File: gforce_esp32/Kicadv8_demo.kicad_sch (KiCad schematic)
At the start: 26 parts, among them J1 USB_C_Receptacle, SW1 TL3215AF160BQ, SW2 TL3215AF160RQ, U1 ESP32-S3-MINI-1U, U2 AP2112K-3.3, U3 LIS3DH

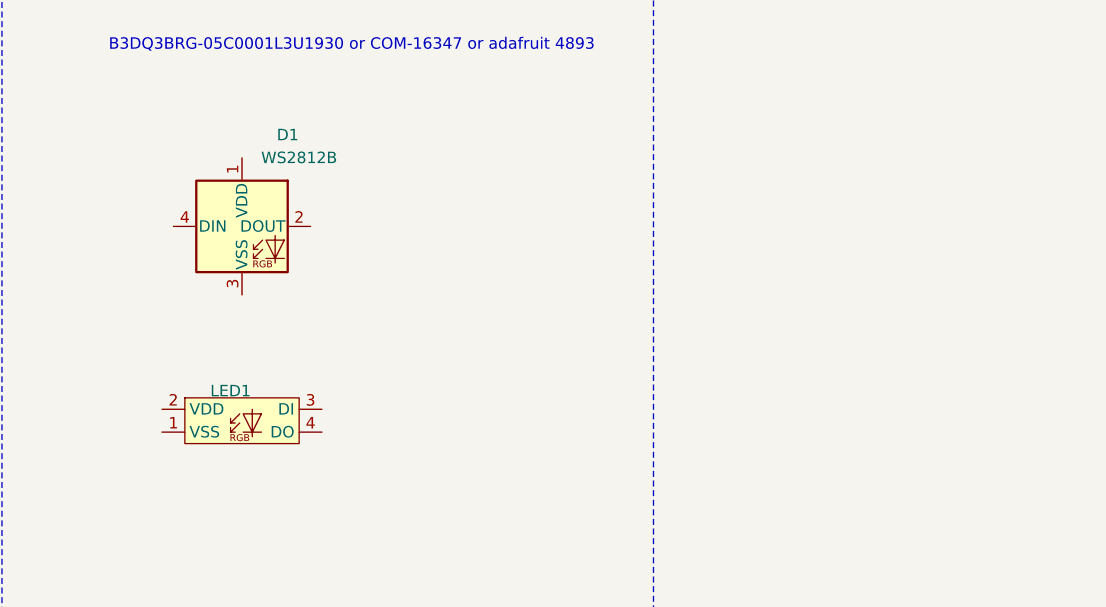
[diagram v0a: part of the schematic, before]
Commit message: gforce_esp32 is newest
added 3d footprint of mcu
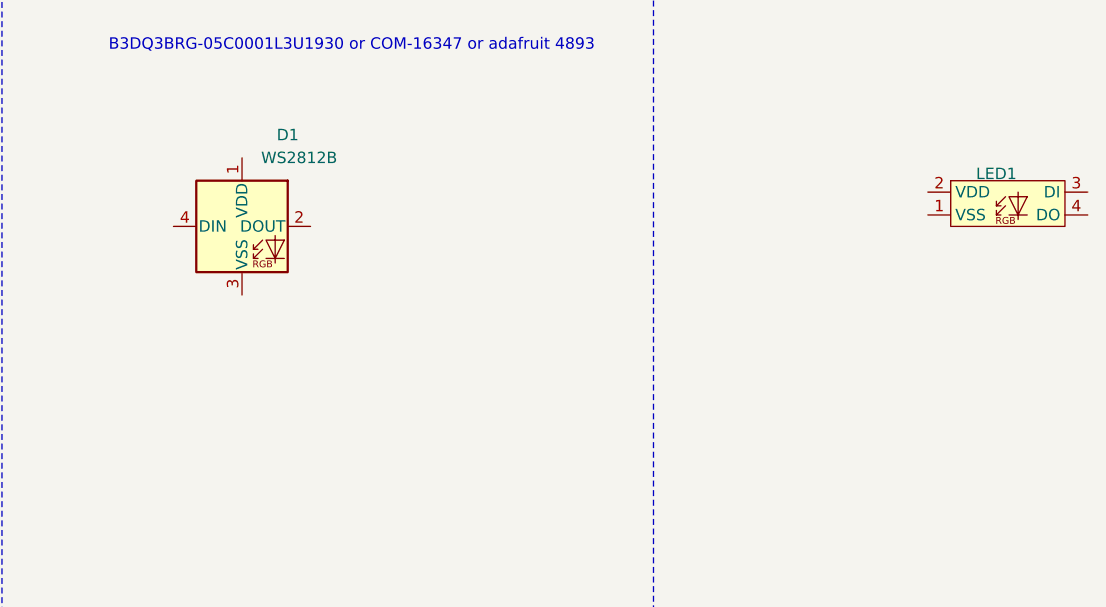
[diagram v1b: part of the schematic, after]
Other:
- moved on the sheet: LED1
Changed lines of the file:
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@@
 	(symbol
 		(lib_id "B3DQ3:B3DQ3BRG")
-		(at 358.14 212.09 0)
+		(at 443.23 187.96 0)
 		(unit 1)
 		(exclude_from_sim no)
@@
 		(dnp no)
 		(property "Reference" "LED1"
-			(at 358.14 208.788 0)
+			(at 443.23 184.658 0)
 			(effects
 				(font
@@
 		)
 		(property "Value" "~"
-			(at 358.14 208.28 0)
+			(at 443.23 184.15 0)
 			(effects
 				(font
@@
 		)
 		(property "Footprint" "B3DQ3BRG_SMT:B3DQ3BRG"
-			(at 363.22 214.63 0)
+			(at 448.31 190.5 0)
 			(effects
 				(font
@@
 		)
 		(property "Datasheet" ""
-			(at 363.22 214.63 0)
+			(at 448.31 190.5 0)
 			(effects
 				(font
@@
 		)
 		(property "Description" ""
-			(at 363.22 214.63 0)
+			(at 448.31 190.5 0)
 			(effects
 				(font

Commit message: layout placing parts
lined up leds
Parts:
- added D10, D11, D12, D13, D14, D15, D16, D17, D18, D19, D2, D20, D21, D22, D23, D24, D25, D26, D27, D28, D29, D3, D30, D31, D32, D33, D34, D35, D36, D37, D38, D39, D4, D40, D5, D6, D7, D8, D9: WS2812B, LED_SMD:LED_WS2812B_PLCC4_5.0x5.0mm_P3.2mm, symbol LED:WS2812B
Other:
- moved on the sheet: D1, LED1

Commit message: SCHEMATIC LEDS MAPPED. FAB NOTES ADDED
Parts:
- removed LED1: ~, B3DQ3BRG_SMT:B3DQ3BRG, symbol B3DQ3:B3DQ3BRG
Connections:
- net +5V: now also D1.1 (VDD), D10.1 (VDD), D11.1 (VDD), D12.1 (VDD), D13.1 (VDD), D14.1 (VDD), D15.1 (VDD), D16.1 (VDD), D17.1 (VDD), D18.1 (VDD), D19.1 (VDD), D2.1 (VDD), D20.1 (VDD), D21.1 (VDD), D22.1 (VDD), D23.1 (VDD), D24.1 (VDD), D25.1 (VDD), D26.1 (VDD), D27.1 (VDD), D28.1 (VDD), D29.1 (VDD), D3.1 (VDD), D30.1 (VDD), D31.1 (VDD), D32.1 (VDD), D33.1 (VDD), D34.1 (VDD), D35.1 (VDD), D36.1 (VDD), D37.1 (VDD), D38.1 (VDD), D39.1 (VDD), D4.1 (VDD), D40.1 (VDD), D5.1 (VDD), D6.1 (VDD), D7.1 (VDD), D8.1 (VDD), D9.1 (VDD)
- net GND: now also D1.3 (VSS), D10.3 (VSS), D11.3 (VSS), D12.3 (VSS), D13.3 (VSS), D14.3 (VSS), D15.3 (VSS), D16.3 (VSS), D17.3 (VSS), D18.3 (VSS), D19.3 (VSS), D2.3 (VSS), D20.3 (VSS), D21.3 (VSS), D22.3 (VSS), D23.3 (VSS), D24.3 (VSS), D25.3 (VSS), D26.3 (VSS), D27.3 (VSS), D28.3 (VSS), D29.3 (VSS), D3.3 (VSS), D30.3 (VSS), D31.3 (VSS), D32.3 (VSS), D33.3 (VSS), D34.3 (VSS), D35.3 (VSS), D36.3 (VSS), D37.3 (VSS), D38.3 (VSS), D39.3 (VSS), D4.3 (VSS), D40.3 (VSS), D5.3 (VSS), D6.3 (VSS), D7.3 (VSS), D8.3 (VSS), D9.3 (VSS)
- net NEOPXL: now also D1.4 (DIN)
- net at D13.2 (DOUT): now also D14.4 (DIN)
- net at D13.4 (DIN): now also D12.2 (DOUT)
- net at D2.2 (DOUT): now also D3.4 (DIN)
- net at D2.4 (DIN): now also D1.2 (DOUT)
- net at D34.2 (DOUT): now also D35.4 (DIN)
- net at D34.4 (DIN): now also D33.2 (DOUT)
- net at D22.2 (DOUT): now also D23.4 (DIN)
- net at D22.4 (DIN): now also D21.2 (DOUT)
- net at D14.2 (DOUT): now also D15.4 (DIN)
- net at D25.2 (DOUT): now also D26.4 (DIN)
- net at D25.4 (DIN): now also D24.2 (DOUT)
- net at D8.2 (DOUT): now also D9.4 (DIN)
- net at D8.4 (DIN): now also D7.2 (DOUT)
- net at D30.2 (DOUT): now also D31.4 (DIN)
- net at D30.4 (DIN): now also D29.2 (DOUT)
- net at D15.2 (DOUT): now also D16.4 (DIN)
- net at D16.2 (DOUT): now also D17.4 (DIN)
- net at D20.2 (DOUT): now also D21.4 (DIN)
- net at D20.4 (DIN): now also D19.2 (DOUT)
- net at D29.4 (DIN): now also D28.2 (DOUT)
- net at D9.2 (DOUT): now also D10.4 (DIN)
- net at D3.2 (DOUT): now also D4.4 (DIN)
- net at D18.2 (DOUT): now also D19.4 (DIN)
- net at D18.4 (DIN): now also D17.2 (DOUT)
- net at D35.2 (DOUT): now also D36.4 (DIN)
- net at D10.2 (DOUT): now also D11.4 (DIN)
- net at D38.2 (DOUT): now also D39.4 (DIN)
- net at D38.4 (DIN): now also D37.2 (DOUT)
- net at D40.4 (DIN): now also D39.2 (DOUT)
- net at D23.2 (DOUT): now also D24.4 (DIN)
- net at D6.2 (DOUT): now also D7.4 (DIN)
- net at D6.4 (DIN): now also D5.2 (DOUT)
- net at D33.4 (DIN): now also D32.2 (DOUT)
- net at D27.2 (DOUT): now also D28.4 (DIN)
- net at D27.4 (DIN): now also D26.2 (DOUT)
- net at D4.2 (DOUT): now also D5.4 (DIN)
- net at D31.2 (DOUT): now also D32.4 (DIN)
- net at D12.4 (DIN): now also D11.2 (DOUT)
- net at D36.2 (DOUT): now also D37.4 (DIN)
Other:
- note added: "axl"
- note removed: "B3DQ3BRG-05C0001L3U1930 or COM-16347 or adafruit 4893"
